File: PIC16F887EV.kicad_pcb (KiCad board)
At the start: 2 copper layers, 100 x 100 mm, 91 parts, among them J1 Conn_01x05_Socket, P1 USB_C_Plug_USB2.0, Q1 2N3904, Q2 2N3904, Q3 2N3904, Q5 2N3904, SW1 SW_Push, SW10 SW_Push, SW11 SW_Push, SW12 SW_Push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

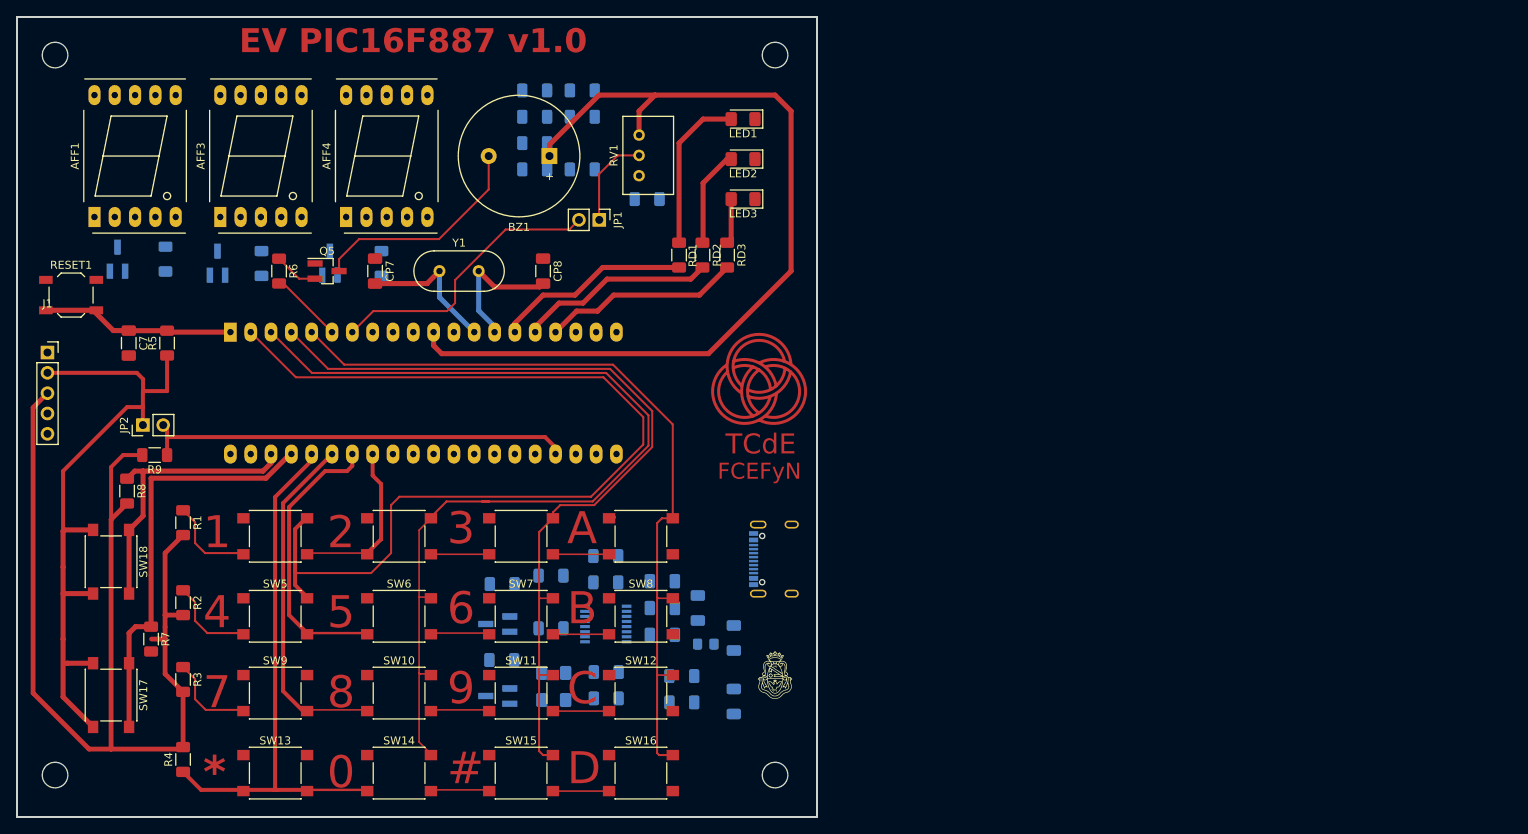
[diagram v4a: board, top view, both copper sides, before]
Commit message: Bloque displays con vías
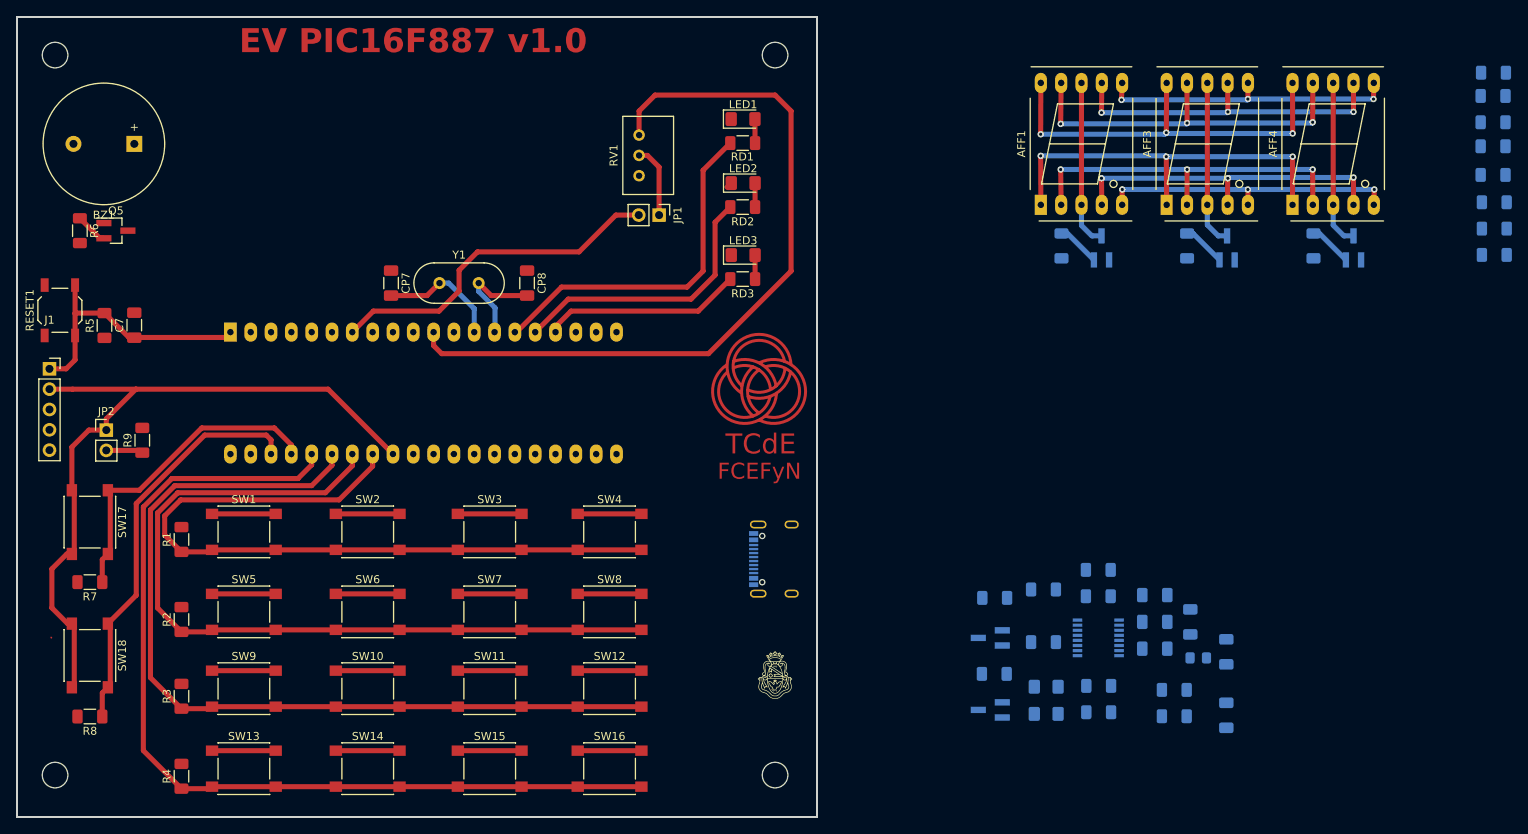
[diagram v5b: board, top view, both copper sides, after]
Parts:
- moved Q3 128.0 mm to (182.3, 44.1)
- moved Q2 126.2 mm to (166.5, 44.1)
- moved Q1 123.0 mm to (150.8, 44.1)
- moved Ra2 120.4 mm to (199.9, 38.4)
- moved Ra3 120.4 mm to (199.9, 41.7)
- moved Ra4 120.4 mm to (199.9, 45.0)
- moved Ra1 119.9 mm to (199.8, 22.2)
- moved AFF4 118.3 mm to (174.7, 38.7)
- moved AFF1 118.3 mm to (143.2, 38.7)
- moved AFF3 118.3 mm to (158.9, 38.7)
- moved RD5 116.5 mm to (177.3, 43.9), turned to -90 degrees
- moved RD4 115.7 mm to (161.5, 43.9), turned to -90 degrees
- moved Ra5 113.9 mm to (199.8, 25.1)
- moved Ra6 113.9 mm to (199.8, 28.4)
- moved Ra8 113.9 mm to (199.8, 35.0)
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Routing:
- net GND: track 135.0 -> 0.51 mm
- net RA0: track 121.9 -> 31.8 mm
- net RA1: track 120.7 -> 31.8 mm
- net RA2: track 105.5 -> 33.6 mm
- net RA3: track 98.8 -> 32.0 mm
- net g: track 0.00 -> 50.7 mm, vias 0 -> 3
- net Net-(JP2-B): track 54.5 -> 4.62 mm
- net e: track 0.00 -> 49.9 mm, vias 0 -> 3
- net f: track 0.00 -> 46.8 mm, vias 0 -> 3
- net RB0: track 46.6 -> 93.1 mm
- net d: track 0.00 -> 44.9 mm, vias 0 -> 3
- net a: track 0.00 -> 42.6 mm, vias 0 -> 3
- net RB2: track 69.6 -> 111.3 mm
- net c: track 0.00 -> 41.8 mm, vias 0 -> 3
- net RB1: track 62.2 -> 102.2 mm
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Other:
- board text removed: "#"
- board text removed: "*"
- board text removed: "0"
- board text removed: "1"
- board text removed: "2"
- board text removed: "3"
- board text removed: "4"
- board text removed: "5"
- board text removed: "6"
- board text removed: "7"
- board text removed: "8"
- board text removed: "9"
- board text removed: "A"
- board text removed: "B"
- board text removed: "C"
- board text removed: "D"

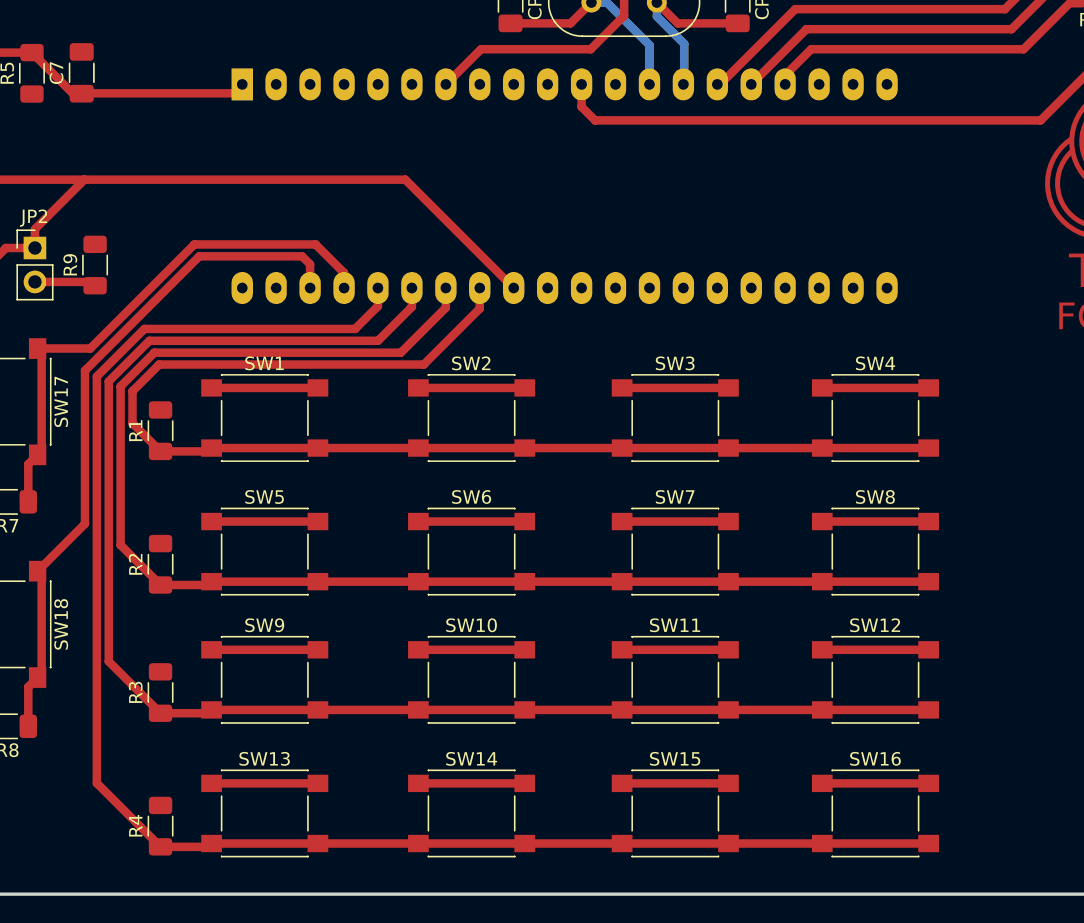
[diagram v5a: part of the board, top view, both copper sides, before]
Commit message: Teclado
Fer hace un rato pifíe con el teclado! acabo de volverlo a rutear más o menos como lo habías ruteado vos, chequealo y cambialo cualquier cosa!
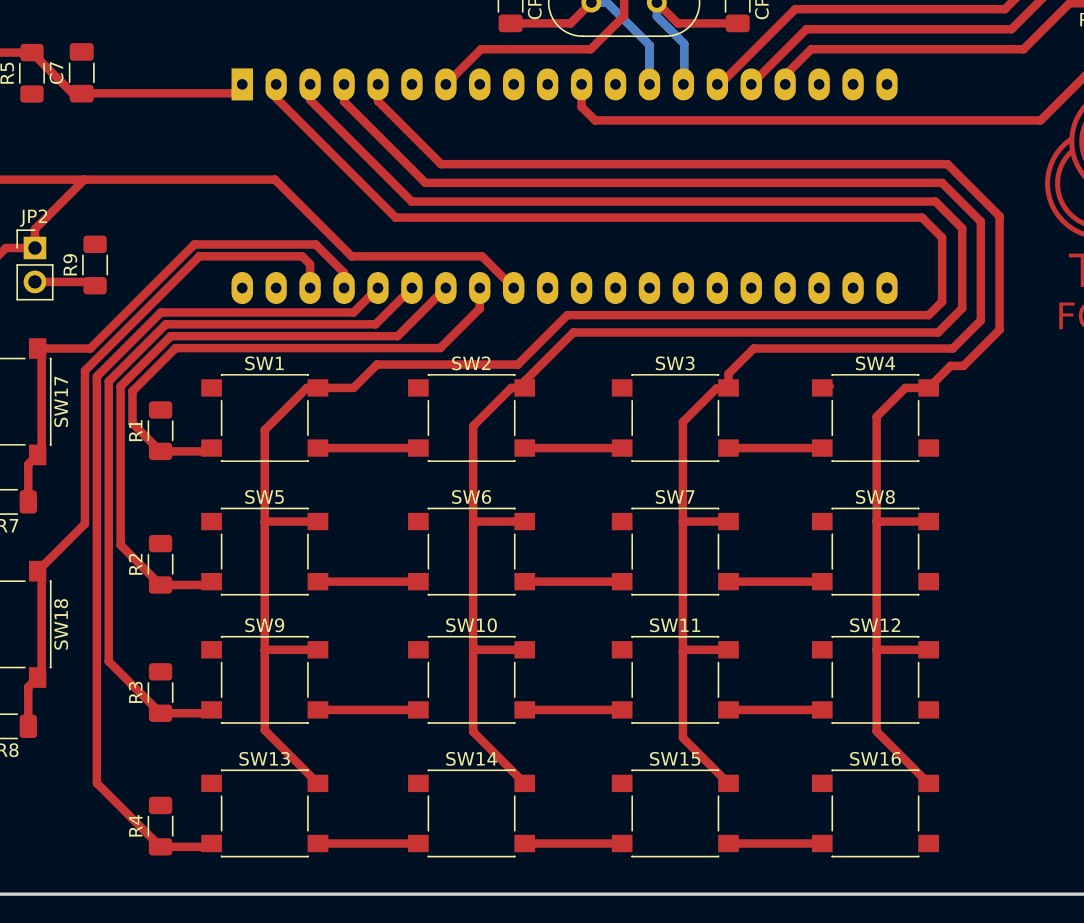
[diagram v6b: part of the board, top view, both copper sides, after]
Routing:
- net RA0: track 31.8 -> 150.8 mm
- net RA1: track 31.8 -> 136.6 mm
- net RA2: track 33.6 -> 121.5 mm
- net RA3: track 32.0 -> 109.0 mm
- net RB1: track 102.2 -> 69.5 mm
- net RB2: track 111.3 -> 78.6 mm
- net RB3: track 119.6 -> 86.9 mm
- net RB0: track 93.1 -> 61.2 mm

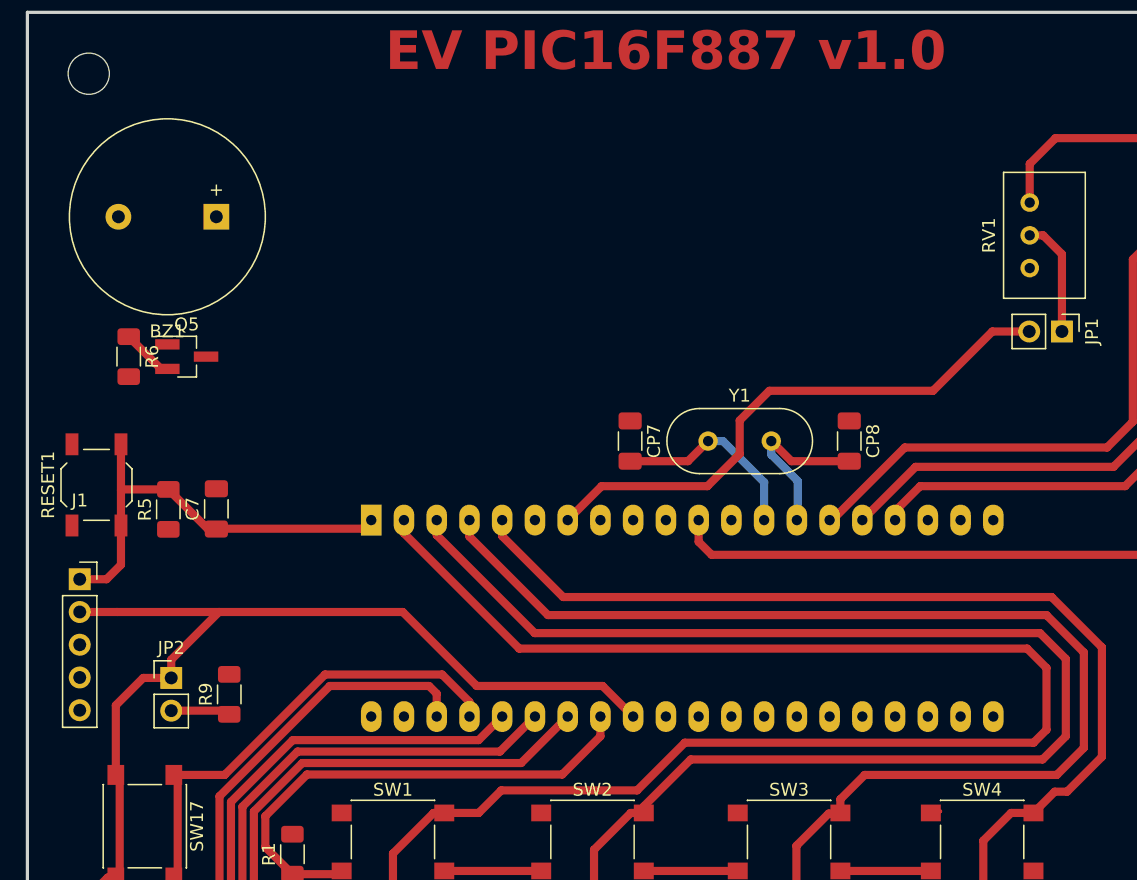
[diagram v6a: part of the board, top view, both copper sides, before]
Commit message: Buzzer y Jumper para Pickit
Ruteo del buzzer y ajuste de espacio para ver si entran los displays en la parte de arriba.
A los 3 displays los dejé mas o menos acomodados a un costado para después ponerlos en la placa y conectar al pic por la capa trasera.
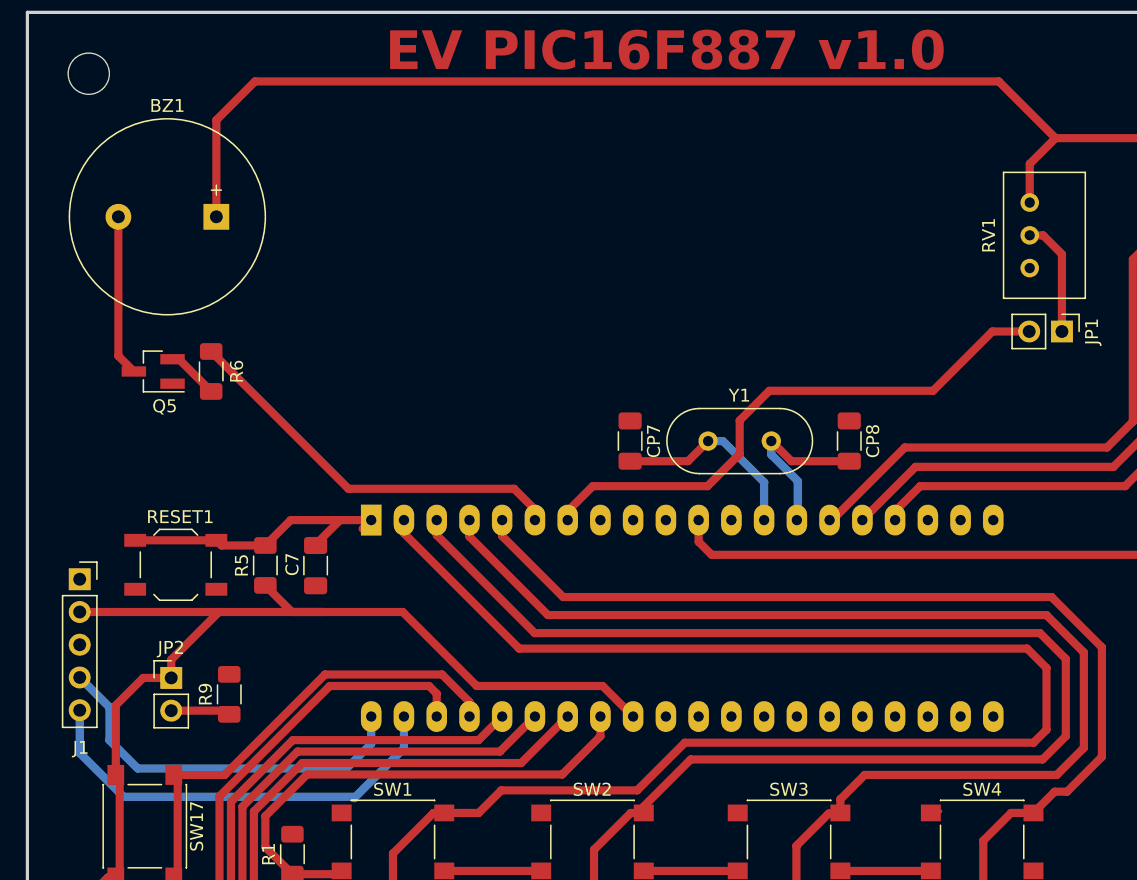
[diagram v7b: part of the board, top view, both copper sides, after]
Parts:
- moved C7 8.87 mm to (37.6, 58.2), turned to -90 degrees
- moved RESET1 8.73 mm to (26.8, 58.1), turned to 180 degrees
- moved R5 8.69 mm to (33.7, 58.1)
- moved R6 6.50 mm to (29.5, 43.1), turned to 90 degrees
- moved Q5 2.84 mm to (25.0, 43.1), turned to 180 degrees
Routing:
- net +5V: track 185.7 -> 266.6 mm
- net ICSPCLK: track 0.00 -> 34.0 mm
- net RA4: track 0.00 -> 31.0 mm
- net ICSPDAT: track 0.00 -> 29.9 mm
- net Net-(BZ1-+): track 0.00 -> 12.5 mm
- net MCLR: track 34.0 -> 23.0 mm

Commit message: Ubicación de Displays
Me están quedando pendientes las 8 Res de cada segmento
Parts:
- moved Q2 104.4 mm to (62.1, 45.7)
- moved RD4 104.4 mm to (57.1, 45.5)
- moved Q1 101.5 mm to (49.4, 45.7)
- moved RD12 101.5 mm to (44.4, 45.5)
- moved AFF4 101.5 mm to (73.2, 40.3)
- moved AFF1 101.5 mm to (41.8, 40.3)
- moved AFF3 101.5 mm to (57.5, 40.3)
- moved Q3 99.4 mm to (83.0, 45.7)
- moved RD5 99.4 mm to (78.0, 45.5), turned to 90 degrees
- moved Ra4 61.1 mm to (140.4, 31.3), turned to -90 degrees
- moved Ra1 59.1 mm to (140.7, 23.6), turned to -90 degrees
- moved Ra8 56.5 mm to (144.4, 23.6), turned to -90 degrees
- moved Ra5 51.9 mm to (147.8, 23.6), turned to -90 degrees
- moved Ra6 48.8 mm to (151.2, 23.7), turned to -90 degrees
- moved Ra7 45.1 mm to (155.3, 23.9), turned to 90 degrees
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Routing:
- net RE2: track 0.00 -> 22.7 mm
- net RE0: track 0.00 -> 20.4 mm
- net RE1: track 0.00 -> 9.74 mm
- net Net-(Q2-C): track 20.8 -> 19.3 mm
- net Net-(Q3-B): track 5.42 -> 4.13 mm
- net RA5: track 44.2 -> 45.2 mm
- net Net-(U1-RA6/OSC2/CLKOUT): track 13.7 -> 12.9 mm
- net Net-(Q3-C): track 20.9 -> 21.5 mm
